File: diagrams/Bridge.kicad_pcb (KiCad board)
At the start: 2 copper layers, 53.5 x 53 mm, 8 parts, among them J1 USB_A, J2 USB_A, J3 USB_A, J4 USB_A, J5 USB_A, U1 WeMos_D1_mini, U2 TSR1-2433E

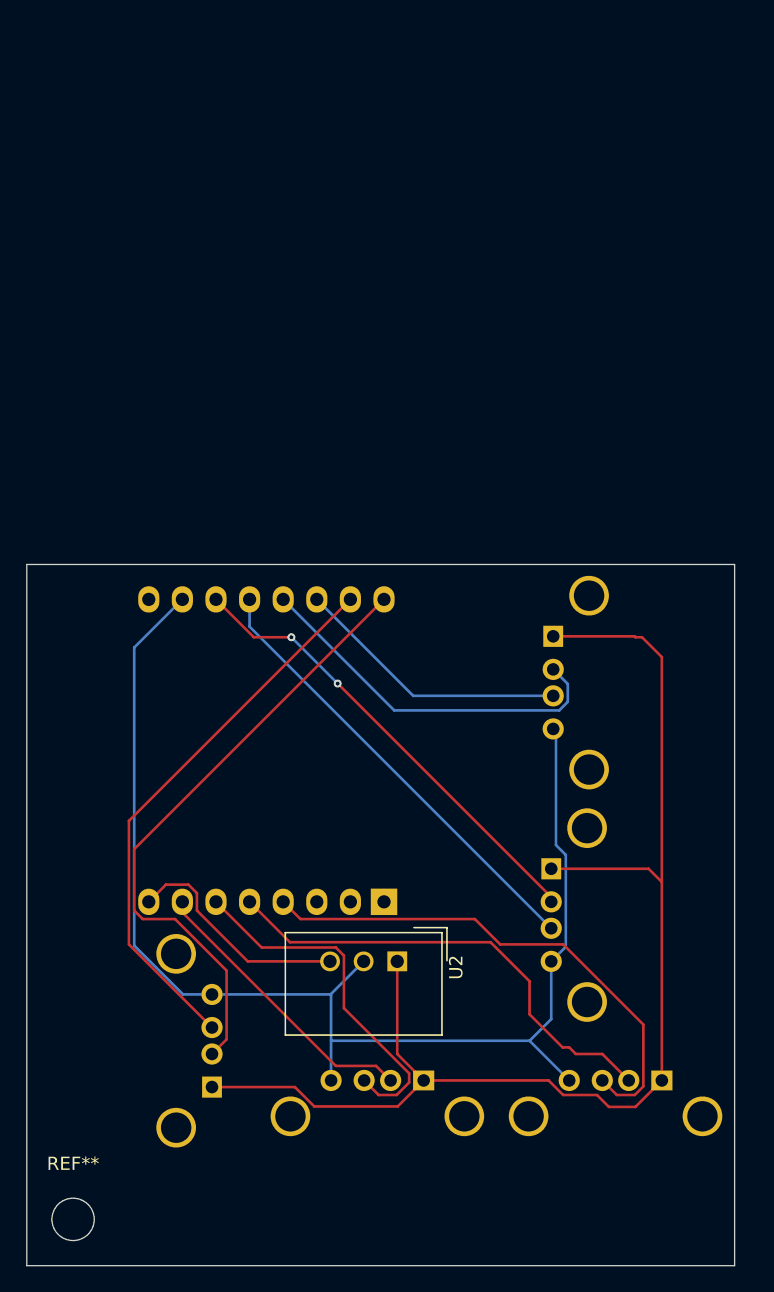
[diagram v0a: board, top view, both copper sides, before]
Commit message: Added drawio diagrams and circuits
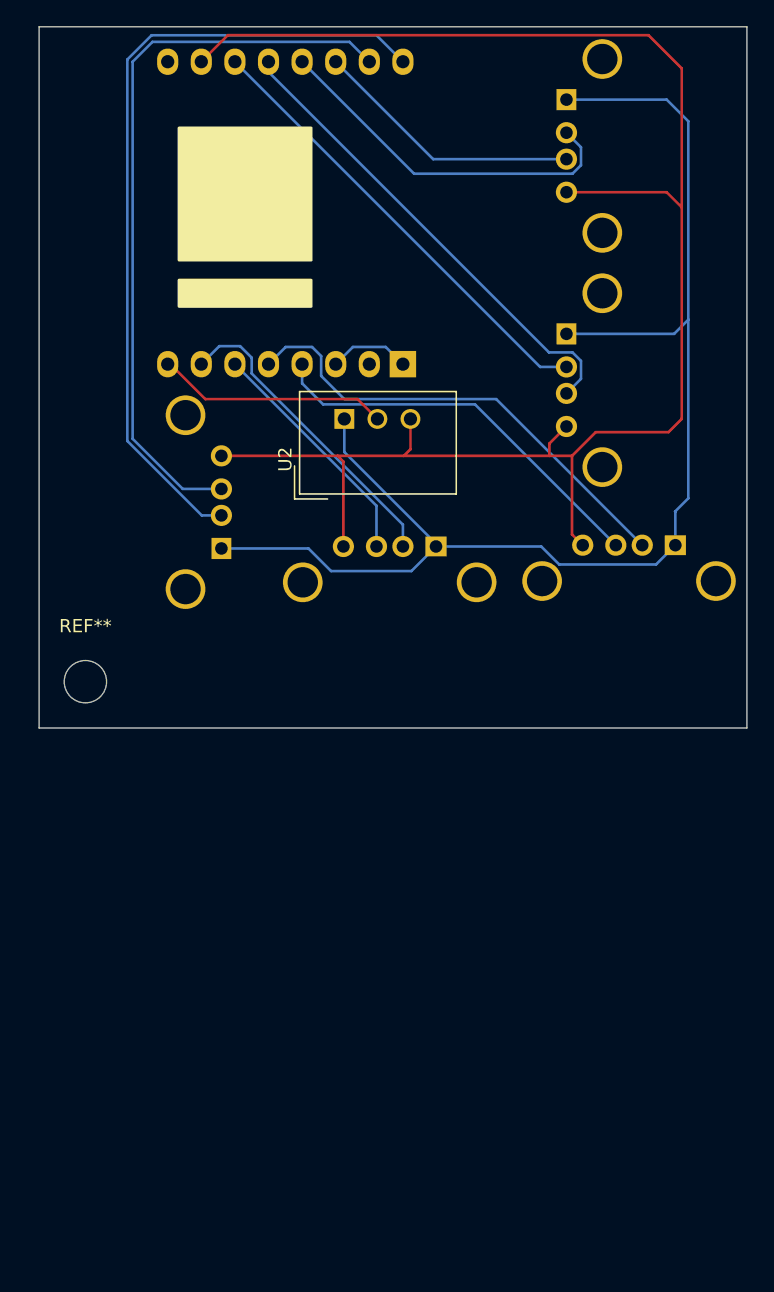
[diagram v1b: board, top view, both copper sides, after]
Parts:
- added G***: LOGO, LOGO, B.Cu at (105.0, 125.5)
- moved J1 40.7 mm to (105.7, 115.3)
- moved U1 40.7 mm to (119.4, 101.4)
- moved REF** 40.7 mm to (95.4, 125.4)
- moved J2 40.6 mm to (131.8, 81.4)
- moved J4 40.5 mm to (140.0, 115.0)
- moved J3 40.4 mm to (131.8, 99.1)
- moved J5 40.4 mm to (121.9, 115.1)
- moved U2 37.7 mm to (115.0, 109.0), turned to 90 degrees
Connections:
- J1 pad 4: Net-(J1-D-) -> Net-(J1-GND)
- J2 pad 4: Net-(J1-D-) -> Net-(J1-GND)
- J3 pad 4: Net-(J1-D-) -> Net-(J1-GND)
- J4 pad 4: Net-(J1-D-) -> Net-(J1-GND)
- J5 pad 4: Net-(J1-D-) -> Net-(J1-GND)
- U1 pad 1: unconnected-(U1-~{RST}-Pad1) -> Net-(U1-D0)
- U1 pad 10: Net-(J1-D-) -> Net-(J1-GND)
- U1 pad 3: unconnected-(U1-D0-Pad3) -> Net-(U1-D0)
- U2 pad 2: Net-(J1-D-) -> Net-(J1-GND)
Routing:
- net Net-(J1-GND): track 0.00 -> 129.7 mm
- net Net-(J1-D-): track 145.4 -> 60.7 mm
- net Net-(J1-D+): track 41.9 -> 55.9 mm
- net Net-(J4-D+): track 39.6 -> 30.2 mm
- net Net-(J5-D+): track 27.2 -> 18.2 mm
- net Net-(U1-D0): track 0.00 -> 6.16 mm
- net Net-(J1-VBUS): track 96.5 -> 102.0 mm
- net Net-(J3-D+): track 34.3 -> 36.3 mm
- net Net-(J5-D-): track 21.8 -> 23.7 mm
- net Net-(J3-D-): track 35.0 -> 34.6 mm, vias 2 -> 0
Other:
- board text added: "Bridge PCB V1.2"
- board text removed: "AutoTF"
- board text removed: "Bridge PCB V1"
